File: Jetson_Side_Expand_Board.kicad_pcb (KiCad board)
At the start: 2 copper layers, 24.1 x 46.7 mm, 16 parts, among them J1 Conn_01x12_Socket, J2 Conn_01x04_Socket, J3 Conn_01x04, J4 Conn_01x02_Pin, J5 Conn_01x02, J6 Conn_01x02_Pin, J7 Conn_01x02, J8 Conn_01x03_Pin, U1 TCAN332G

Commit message: セラコンのGND
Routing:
- net GND: track 33.6 -> 35.8 mm

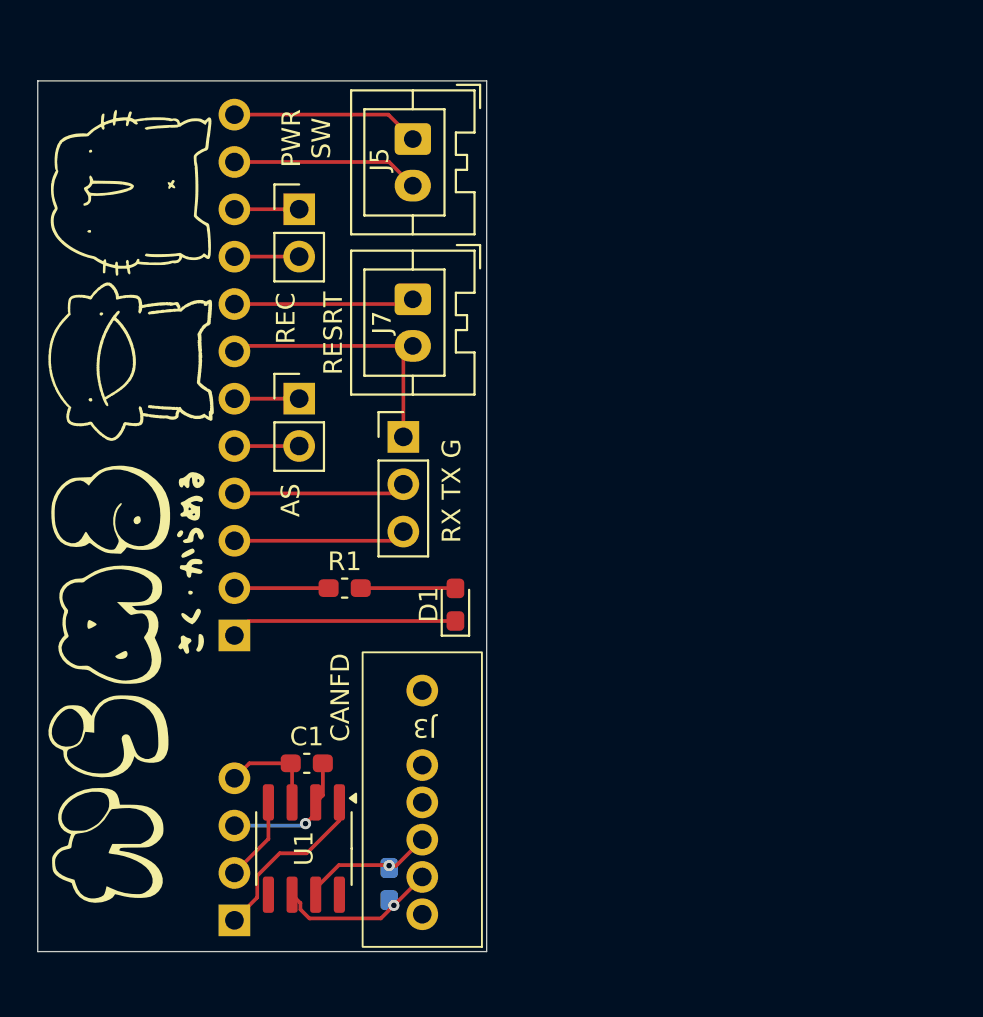
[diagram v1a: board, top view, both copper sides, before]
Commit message: 5Vを24Vからレギュレータで作る
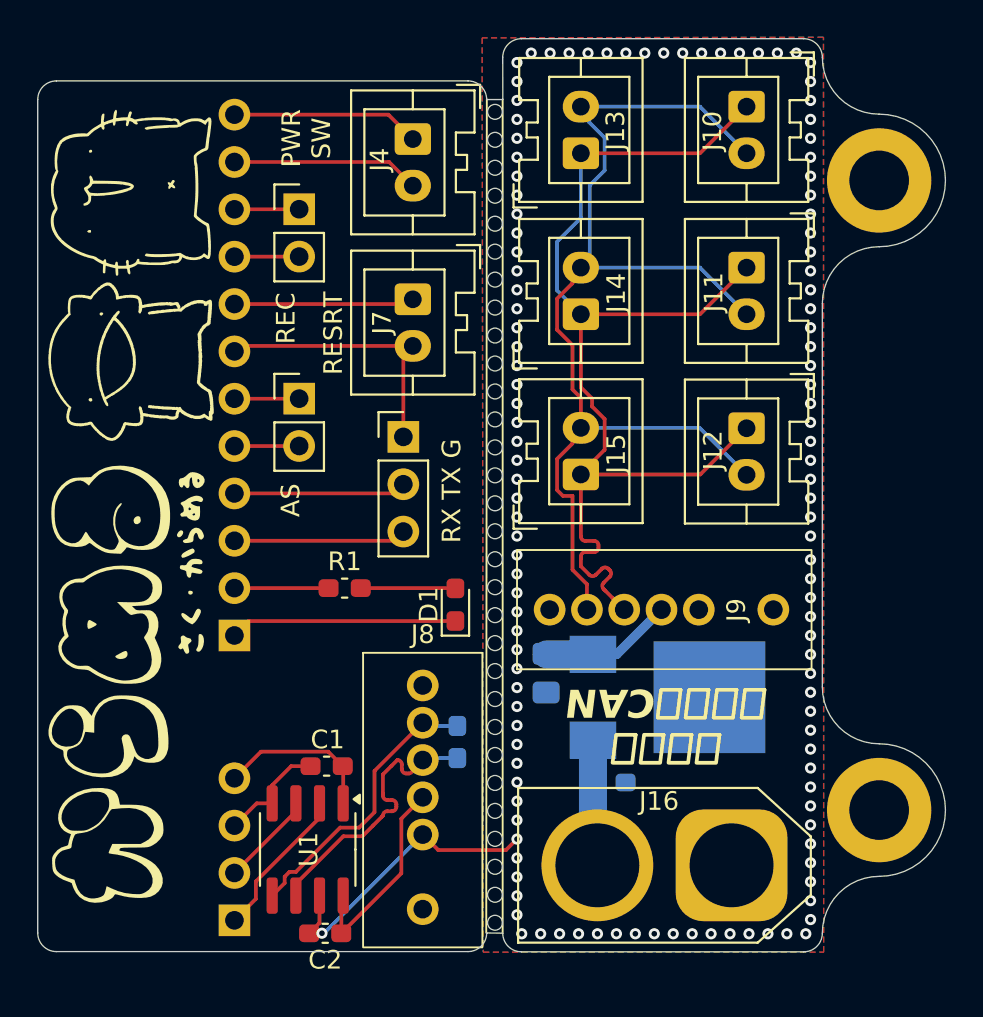
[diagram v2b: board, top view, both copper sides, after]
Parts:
- removed the J3 at (126.2, 109.1)
- added C2: 100n, Capacitor_SMD:C_0603_1608Metric_Pad1.08x0.95mm_HandSolder, F.Cu at (121.0, 116.3)
- added C3: 10u, Capacitor_SMD:C_0805_2012Metric_Pad1.18x1.45mm_HandSolder, B.Cu at (132.9, 102.4)
- added C4: 100n, Capacitor_SMD:C_0603_1608Metric_Pad1.08x0.95mm_HandSolder, B.Cu at (136.3, 108.2)
- added IC1: NJM2391DL1-05-TE1, NJM2391:TO-252-3-L1_1, B.Cu at (141.6, 103.6)
- added J10: Conn_01x02, Connector_JST:JST_XA_B02B-XASK-1_1x02_P2.50mm_Vertical, F.Cu at (143.6, 72.0)
- added J11: Conn_01x02, Connector_JST:JST_XA_B02B-XASK-1_1x02_P2.50mm_Vertical, F.Cu at (143.6, 80.6)
- added J12: Conn_01x02, Connector_JST:JST_XA_B02B-XASK-1_1x02_P2.50mm_Vertical, F.Cu at (143.6, 89.2)
- added J13: Conn_01x02, Connector_JST:JST_XA_B02B-XASK-1_1x02_P2.50mm_Vertical, F.Cu at (134.7, 74.5)
- added J14: Conn_01x02, Connector_JST:JST_XA_B02B-XASK-1_1x02_P2.50mm_Vertical, F.Cu at (134.7, 83.1)
- added J15: Conn_01x02, Connector_JST:JST_XA_B02B-XASK-1_1x02_P2.50mm_Vertical, F.Cu at (134.7, 91.7)
- added J16: 24V, Connector_AMASS:AMASS_XT60-M_1x02_P7.20mm_Vertical, F.Cu at (142.8, 112.7)
- added J8: Conn_01x04, e-CON:e-CON_1×04, F.Cu at (126.3, 109.2)
- added J9: e-CON, e-CON:e-CON_1×04, F.Cu at (139.2, 98.9)
- added REF**: MountingHole_3.2mm_M3_DIN965_Pad, MountingHole:MountingHole_3.2mm_M3_DIN965_Pad, F.Cu at (150.7, 109.7)
- added REF**: MountingHole_3.2mm_M3_DIN965_Pad, MountingHole:MountingHole_3.2mm_M3_DIN965_Pad, F.Cu at (150.7, 75.9)
- U1: value TCAN332G -> ~
- moved R2 8.45 mm to (128.1, 106.0), turned to 90 degrees
- moved C1 1.08 mm to (121.1, 107.3), turned to 180 degrees
- moved U1 0.21 mm to (120.1, 111.8)
- renumbered J6 to J3, J5 to J4, J4 to J5, J8 to J6
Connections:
- U1 pad 1: /CAN_TX -> +3.3V
- U1 pad 2: GND -> /CAN_TX
- U1 pad 3: +3.3V -> /CAN_RX
- U1 pad 4: /CAN_RX -> GND
- U1 pad 5: unconnected-(U1-NC-Pad5) -> /CAN-
- U1 pad 6: /CAN- -> /CAN+
- U1 pad 7: /CAN+ -> GND1
- U1 pad 8: unconnected-(U1-NC-Pad8) -> +5V
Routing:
- net /DCDC5V/CAN-: track 0.00 -> 60.4 mm
- net /DCDC5V/CAN+: track 0.00 -> 60.2 mm
- net +5V: track 0.00 -> 18.4 mm
- net GND1: track 0.00 -> 16.2 mm, vias 0 -> 124
- net /CAN+: track 7.67 -> 15.4 mm, vias 1 -> 0
- net VDD: track 0.00 -> 6.82 mm
- net /CAN-: track 9.37 -> 15.3 mm, vias 1 -> 0
- net +3.3V: track 5.48 -> 8.73 mm
- net GND: track 35.8 -> 34.3 mm, vias 1 -> 0
- net /CAN_TX: track 9.51 -> 8.17 mm
- net /CAN_RX: track 4.54 -> 5.10 mm
- added copper zone on B.Cu, net GND1
- added copper zone on F.Cu, net GND1
- added copper zone on In1.Cu, net GND1
- added copper zone on In2.Cu, net GND1
- added copper zone on In3.Cu, net GND1
- added copper zone on In4.Cu, net GND1
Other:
- board size 24.1 x 46.7 mm -> 48.7 x 49 mm
- copper layers 2 -> 6
- board text added: "でーれー あぶないCAN"
- board text removed: "CANFD"
